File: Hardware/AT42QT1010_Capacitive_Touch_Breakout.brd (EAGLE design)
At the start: 25.4 x 33 mm, 30 parts, among them Q1 NPN, U1 AT42QT1010UDFN

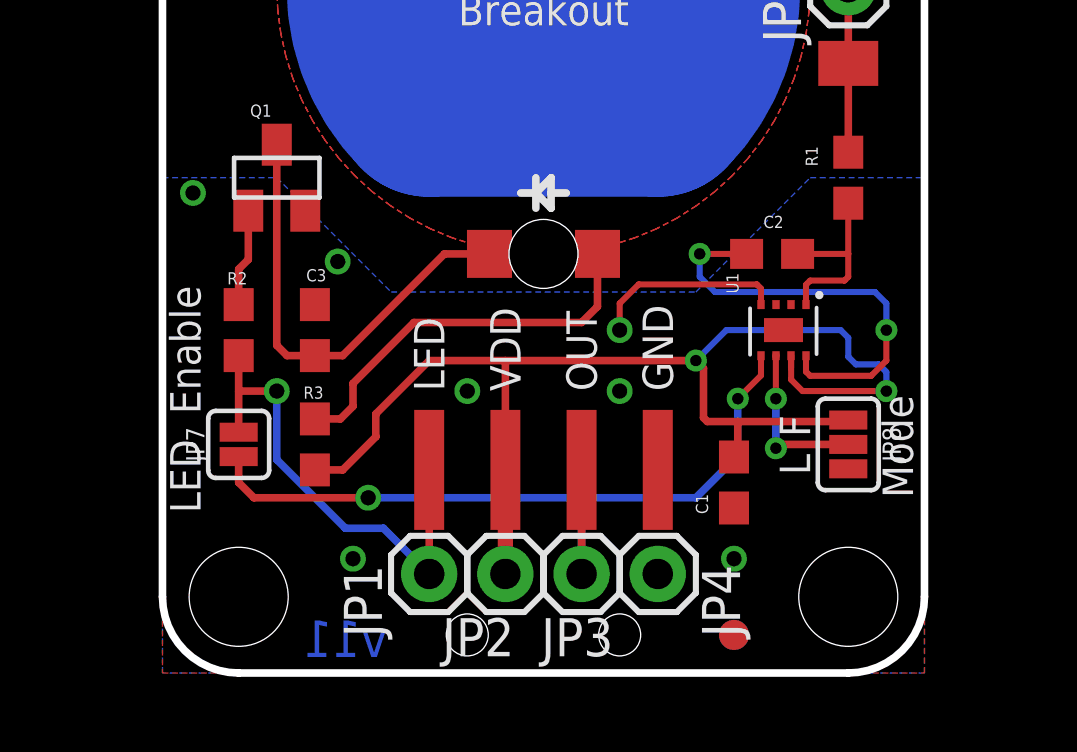
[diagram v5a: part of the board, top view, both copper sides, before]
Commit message: Update from Review Feedback
Added better text to the schematic to explain slow/fast mode. Got rid of
an uneccesary VCC trace, added more gnd vias and changed all vias to 15
mil for consistency.
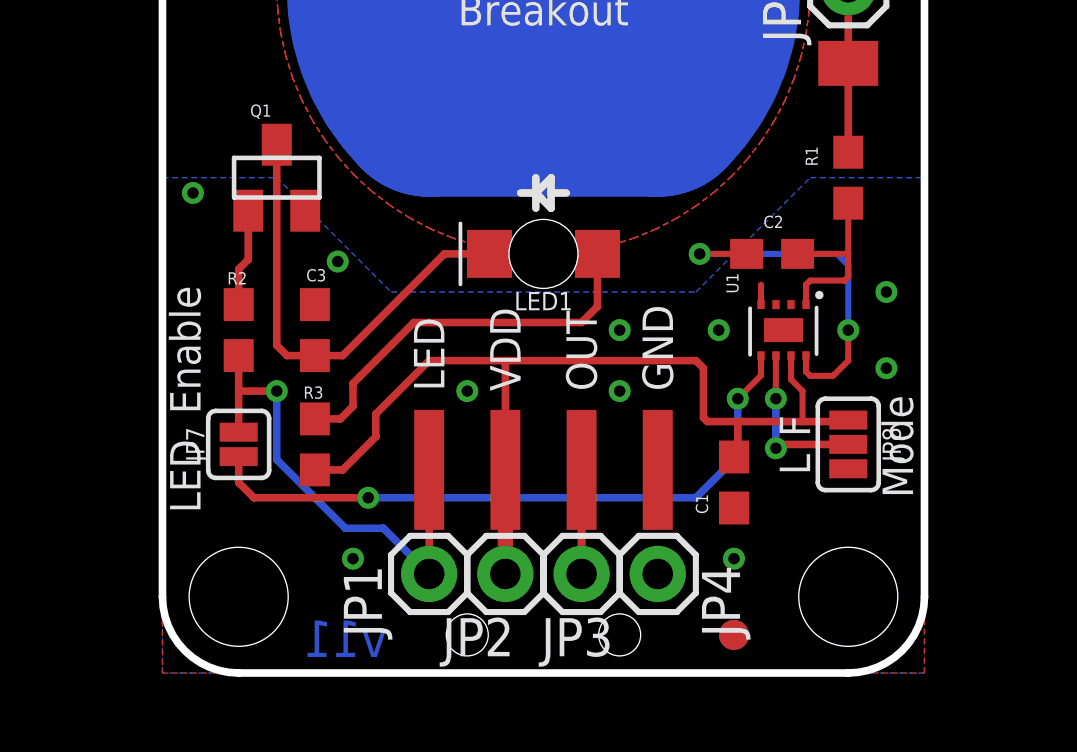
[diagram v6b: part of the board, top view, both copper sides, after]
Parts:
- removed LOGO3: LOGO-SFESK, SparkFun-Aesthetics:SFE-LOGO-FLAME
- added LOGO1: SFE_LOGO_FLAME.3_INCH, SparkFun-Aesthetics:SFE_LOGO_FLAME_.3
- LED1: value GREEN -> Green
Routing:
- net VCC: track 42.9 -> 32.7 mm, vias 2 -> 0
- net GND: track 6.45 -> 0.66 mm, vias 7 -> 10
- net N$4: track 14.4 -> 12.1 mm
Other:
- board text removed: "Knock out"
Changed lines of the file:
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@@
 <wire x1="22.86" y1="0" x2="2.54" y2="0" width="0.254" layer="20"/>
 <wire x1="2.54" y1="0" x2="0" y2="2.54" width="0.254" layer="20" curve="-90"/>
-<text x="25.4" y="33.02" size="1.27" layer="51" font="vector" ratio="15">Knock out</text>
 <text x="12.7" y="-7.62" size="1.27" layer="21" font="vector" ratio="15" align="bottom-center">The 0.09055118 in. (2.3mm) hole is NPTH hole</text>
 <rectangle x1="24.511" y1="9.779" x2="25.019" y2="10.922" layer="41"/>
@@
 <element name="STANDOFF3" library="SparkFun-Electromechanical" package="STAND-OFF" value="STAND-OFF" x="22.86" y="30.48"/>
 <element name="STANDOFF4" library="SparkFun-Electromechanical" package="STAND-OFF" value="STAND-OFF" x="2.54" y="30.48"/>
-<element name="LOGO3" library="SparkFun-Aesthetics" package="SFE-LOGO-FLAME" value="LOGO-SFESK" x="2.54" y="17.78" rot="MR0"/>
 <element name="JP1" library="SparkFun-Connectors" package="1X01" value="M01PTH" x="8.89" y="3.302" smashed="yes">
 <attribute name="NAME" x="7.3152" y="1.1938" size="1.27" layer="25" rot="R90"/>
@@
 </element>
 <element name="JP6" library="SparkFun-Connectors" package="1X04-SMD_LONG" value="SMD" x="12.7" y="1.27"/>
-<element name="LED1" library="SparkFun-LED" package="LED-1206-BOTTOM" value="GREEN" x="12.7" y="13.97" rot="R180"/>
+<element name="LED1" library="SparkFun-LED" package="LED-1206-BOTTOM" value="Green" x="12.7" y="13.97" rot="R180">
+<attribute name="PROD_ID" value="DIO-11076" x="12.7" y="13.97" size="1.778" layer="27" rot="R180" display="off"/>
+<attribute name="VALUE" value="Green" x="12.7" y="13.97" size="1.778" layer="27" rot="R180" display="off"/>
+</element>
 <element name="FID1" library="SparkFun-Aesthetics" package="FIDUCIAL-1X2" value="FIDUCIAL1X2" x="6.35" y="31.75"/>
 <element name="FID2" library="SparkFun-Aesthetics" package="FIDUCIAL-1X2" value="FIDUCIAL1X2" x="19.05" y="1.27"/>
@@
 <element name="JP7" library="SparkFun-Jumpers" package="SMT-JUMPER_2_NO_SILK" value="JUMPER-SMT_2_NO_SILK" x="2.54" y="7.62" rot="R90"/>
 <element name="LOGO5" library="SparkFun-Aesthetics" package="SFE_LOGO_NAME_WEB" value="SFE_LOGO_NAME_WEB" x="3.81" y="25.4"/>
+<element name="LOGO1" library="SparkFun-Aesthetics" package="SFE_LOGO_FLAME_.3" value="SFE_LOGO_FLAME.3_INCH" x="15.24" y="19.558" rot="MR0"/>
 </elements>
 <signals>
@@
 <wire x1="18.034" y1="10.16" x2="17.78" y2="10.414" width="0.254" layer="1"/>
 <wire x1="20.951" y1="10.5784" x2="20.951" y2="10.164" width="0.2032" layer="1"/>
-<wire x1="21.336" y1="9.398" x2="24.13" y2="9.398" width="0.2032" layer="1"/>
-<via x="24.13" y="9.398" extent="1-16" drill="0.381"/>
-<wire x1="24.13" y1="9.398" x2="24.13" y2="10.033" width="0.2032" layer="16"/>
-<wire x1="24.13" y1="10.033" x2="23.876" y2="10.287" width="0.2032" layer="16"/>
-<wire x1="23.876" y1="10.287" x2="23.114" y2="10.287" width="0.2032" layer="16"/>
-<wire x1="23.114" y1="10.287" x2="22.86" y2="10.541" width="0.2032" layer="16"/>
-<wire x1="22.86" y1="10.541" x2="22.86" y2="11.176" width="0.2032" layer="16"/>
-<wire x1="22.86" y1="11.176" x2="22.606" y2="11.43" width="0.2032" layer="16"/>
-<wire x1="22.606" y1="11.43" x2="18.796" y2="11.43" width="0.2032" layer="16"/>
-<wire x1="18.796" y1="11.43" x2="17.78" y2="10.414" width="0.2032" layer="16"/>
-<via x="17.78" y="10.414" extent="1-16" drill="0.381"/>
+<wire x1="21.336" y1="9.398" x2="21.336" y2="8.382" width="0.2032" layer="1"/>
 <wire x1="18.034" y1="8.509" x2="18.161" y2="8.382" width="0.254" layer="1"/>
 <wire x1="18.161" y1="8.382" x2="19.177" y2="8.382" width="0.254" layer="1"/>
 <wire x1="19.177" y1="8.382" x2="19.177" y2="7.327" width="0.254" layer="1"/>
 <wire x1="19.177" y1="7.327" x2="19.05" y2="7.2" width="0.254" layer="1"/>
-<wire x1="19.177" y1="8.382" x2="22.8092" y2="8.382" width="0.254" layer="1"/>
+<wire x1="19.177" y1="8.382" x2="21.336" y2="8.382" width="0.254" layer="1"/>
+<wire x1="21.336" y1="8.382" x2="22.8092" y2="8.382" width="0.254" layer="1"/>
 <wire x1="22.8092" y1="8.382" x2="22.86" y2="8.4328" width="0.254" layer="1"/>
 <wire x1="21.336" y1="9.398" x2="20.955" y2="9.779" width="0.2032" layer="1"/>
@@
 </polygon>
 <contactref element="JP6" pad="4"/>
-<via x="6.35" y="3.81" extent="1-16" drill="0.508"/>
-<via x="19.05" y="3.81" extent="1-16" drill="0.508"/>
-<via x="5.842" y="13.716" extent="1-16" drill="0.508"/>
+<via x="6.35" y="3.81" extent="1-16" drill="0.381"/>
+<via x="19.05" y="3.81" extent="1-16" drill="0.381"/>
+<via x="5.842" y="13.716" extent="1-16" drill="0.381"/>
 <contactref element="JP8" pad="3"/>
-<via x="10.16" y="9.398" extent="1-16" drill="0.508"/>
-<via x="15.24" y="9.398" extent="1-16" drill="0.508"/>
-<via x="1.016" y="16.002" extent="1-16" drill="0.508"/>
-<via x="15.24" y="11.43" extent="1-16" drill="0.508"/>
-<wire x1="19.951" y1="12.2816" x2="19.951" y2="12.815" width="0.2032" layer="1"/>
-<wire x1="15.875" y1="12.954" x2="15.24" y2="12.319" width="0.2032" layer="1"/>
-<wire x1="15.24" y1="12.319" x2="15.24" y2="11.43" width="0.2032" layer="1"/>
-<wire x1="19.951" y1="12.815" x2="19.812" y2="12.954" width="0.2032" layer="1"/>
-<wire x1="19.812" y1="12.954" x2="15.875" y2="12.954" width="0.2032" layer="1"/>
+<via x="10.16" y="9.398" extent="1-16" drill="0.381"/>
+<via x="15.24" y="9.398" extent="1-16" drill="0.381"/>
+<via x="1.016" y="16.002" extent="1-16" drill="0.381"/>
+<via x="15.24" y="11.43" extent="1-16" drill="0.381"/>
+<via x="18.542" y="11.43" extent="1-16" drill="0.381"/>
+<via x="24.13" y="12.7" extent="1-16" drill="0.381"/>
+<via x="24.13" y="10.16" extent="1-16" drill="0.381"/>
+<wire x1="19.951" y1="12.2816" x2="19.951" y2="12.942" width="0.2032" layer="1"/>
 </signal>
 <signal name="OUT">
 <contactref element="JP6" pad="3"/>
 <contactref element="JP3" pad="1"/>
-<via x="6.858" y="5.842" extent="1-16" drill="0.508"/>
+<via x="6.858" y="5.842" extent="1-16" drill="0.381"/>
 <wire x1="2.54" y1="6.35" x2="3.048" y2="5.842" width="0.254" layer="1"/>
 <contactref element="U1" pad="5"/>
@@
 <contactref element="JP6" pad="1"/>
 <contactref element="JP1" pad="1"/>
-<via x="3.81" y="9.398" extent="1-16" drill="0.508"/>
+<via x="3.81" y="9.398" extent="1-16" drill="0.381"/>
 <wire x1="2.54" y1="9.398" x2="2.54" y2="10.58" width="0.254" layer="1"/>
 <wire x1="3.81" y1="9.398" x2="2.54" y2="9.398" width="0.254" layer="1"/>
@@
 <wire x1="21.451" y1="10.5784" x2="21.451" y2="10.045" width="0.2032" layer="1"/>
 <wire x1="19.47" y1="13.97" x2="19.558" y2="13.97" width="0.254" layer="1"/>
-<via x="24.13" y="11.43" extent="1-16" drill="0.381"/>
-<wire x1="24.13" y1="10.414" x2="24.13" y2="11.43" width="0.2032" layer="1"/>
-<wire x1="24.13" y1="11.43" x2="24.13" y2="12.319" width="0.2032" layer="16"/>
-<wire x1="24.13" y1="12.319" x2="23.749" y2="12.7" width="0.2032" layer="16"/>
-<wire x1="23.749" y1="12.7" x2="18.415" y2="12.7" width="0.2032" layer="16"/>
+<via x="22.86" y="11.43" extent="1-16" drill="0.381"/>
+<wire x1="22.86" y1="10.414" x2="22.86" y2="11.43" width="0.2032" layer="1"/>
 <wire x1="21.451" y1="10.045" x2="21.59" y2="9.906" width="0.2032" layer="1"/>
-<wire x1="21.59" y1="9.906" x2="23.622" y2="9.906" width="0.2032" layer="1"/>
-<wire x1="23.622" y1="9.906" x2="24.13" y2="10.414" width="0.2032" layer="1"/>
-<wire x1="18.415" y1="12.7" x2="17.907" y2="13.208" width="0.2032" layer="16"/>
-<wire x1="17.907" y1="13.208" x2="17.907" y2="13.97" width="0.2032" layer="16"/>
+<wire x1="21.59" y1="9.906" x2="22.352" y2="9.906" width="0.2032" layer="1"/>
+<wire x1="22.352" y1="9.906" x2="22.86" y2="10.414" width="0.2032" layer="1"/>
 <via x="17.907" y="13.97" extent="1-16" drill="0.381"/>
 <wire x1="17.907" y1="13.97" x2="19.47" y2="13.97" width="0.2032" layer="1"/>
+<wire x1="22.86" y1="11.43" x2="22.86" y2="13.589" width="0.2032" layer="16"/>
+<wire x1="22.86" y1="13.589" x2="22.479" y2="13.97" width="0.2032" layer="16"/>
+<wire x1="22.479" y1="13.97" x2="17.907" y2="13.97" width="0.2032" layer="16"/>
 </signal>
 <signal name="N$5">
